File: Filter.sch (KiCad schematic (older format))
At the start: 3 parts

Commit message: Corrected connectors.
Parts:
- C9: footprint (none) -> Capacitor_SMD:C_0603_1608Metric
- R10, R11: footprint (none) -> Resistor_SMD:R_0603_1608Metric
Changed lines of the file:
@@
 F 0 "R16" H 4470 2346 50  0000 L CNN
 F 1 "10k" H 4470 2255 50  0000 L CNN
-F 2 "" V 4330 2300 50  0001 C CNN
+F 2 "Resistor_SMD:R_0603_1608Metric" V 4330 2300 50  0001 C CNN
 F 3 "~" H 4400 2300 50  0001 C CNN
 	1    4400 2300
@@
 F 0 "R15" V 3943 2550 50  0000 C CNN
 F 1 "10k" V 4034 2550 50  0000 C CNN
-F 2 "" V 4080 2550 50  0001 C CNN
+F 2 "Resistor_SMD:R_0603_1608Metric" V 4080 2550 50  0001 C CNN
 F 3 "~" H 4150 2550 50  0001 C CNN
 	1    4150 2550
@@
 F 0 "C11" H 4515 2846 50  0000 L CNN
 F 1 "10n" H 4515 2755 50  0000 L CNN
-F 2 "" H 4438 2650 50  0001 C CNN
+F 2 "Capacitor_SMD:C_0603_1608Metric" H 4438 2650 50  0001 C CNN
 F 3 "~" H 4400 2800 50  0001 C CNN
 	1    4400 2800

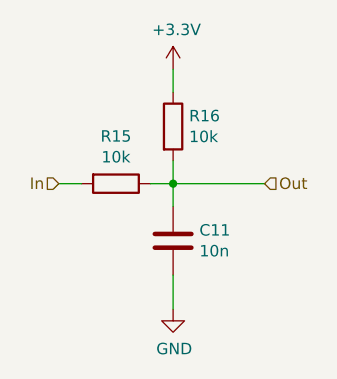
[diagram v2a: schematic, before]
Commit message: Redesigned around G431.
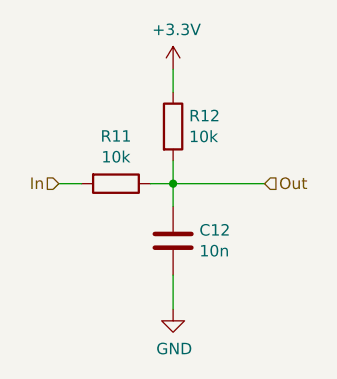
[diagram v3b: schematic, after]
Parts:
- renumbered C9 to C11, R11 to R10, R10 to R9
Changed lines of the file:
@@
 $Descr A4 11693 8268
 encoding utf-8
-Sheet 4 6
+Sheet 3 13
 Title ""
 Date ""
@@
 AR Path="/601E4198/601E449D" Ref="R?"  Part="1"
 AR Path="/601EC842/601E449D" Ref="R?"  Part="1"
-AR Path="/601ED892/601E449D" Ref="R11"  Part="1"
+AR Path="/601ED892/601E449D" Ref="R10"  Part="1"
 AR Path="/601EE918/601E449D" Ref="R?"  Part="1"
-AR Path="/601EF983/601E449D" Ref="R16"  Part="1"
+AR Path="/601EF983/601E449D" Ref="R12"  Part="1"
 AR Path="/601F09BE/601E449D" Ref="R?"  Part="1"
 AR Path="/601F1A3B/601E449D" Ref="R?"  Part="1"
@@
 AR Path="/601F6AC3/601E449D" Ref="R?"  Part="1"
 AR Path="/601F7B55/601E449D" Ref="R?"  Part="1"
-F 0 "R16" H 4470 2346 50  0000 L CNN
+AR Path="/6027857A/601E449D" Ref="R14"  Part="1"
+AR Path="/603499C2/601E449D" Ref="R16"  Part="1"
+AR Path="/603603F4/601E449D" Ref="R18"  Part="1"
+AR Path="/60382A0F/601E449D" Ref="R20"  Part="1"
+AR Path="/60398ACA/601E449D" Ref="R22"  Part="1"
+AR Path="/603AB740/601E449D" Ref="R24"  Part="1"
+AR Path="/603B0EF8/601E449D" Ref="R26"  Part="1"
+AR Path="/603B693F/601E449D" Ref="R28"  Part="1"
+AR Path="/603E1705/601E449D" Ref="R30"  Part="1"
+AR Path="/603E7B18/601E449D" Ref="R32"  Part="1"
+F 0 "R12" H 4470 2346 50  0000 L CNN
 F 1 "10k" H 4470 2255 50  0000 L CNN
 F 2 "Resistor_SMD:R_0603_1608Metric" V 4330 2300 50  0001 C CNN
@@
 AR Path="/601E4198/601E490B" Ref="R?"  Part="1"
 AR Path="/601EC842/601E490B" Ref="R?"  Part="1"
-AR Path="/601ED892/601E490B" Ref="R10"  Part="1"
+AR Path="/601ED892/601E490B" Ref="R9"  Part="1"
 AR Path="/601EE918/601E490B" Ref="R?"  Part="1"
-AR Path="/601EF983/601E490B" Ref="R15"  Part="1"
+AR Path="/601EF983/601E490B" Ref="R11"  Part="1"
 AR Path="/601F09BE/601E490B" Ref="R?"  Part="1"
 AR Path="/601F1A3B/601E490B" Ref="R?"  Part="1"
@@
 AR Path="/601F6AC3/601E490B" Ref="R?"  Part="1"
 AR Path="/601F7B55/601E490B" Ref="R?"  Part="1"
-F 0 "R15" V 3943 2550 50  0000 C CNN
+AR Path="/6027857A/601E490B" Ref="R13"  Part="1"
+AR Path="/603499C2/601E490B" Ref="R15"  Part="1"
+AR Path="/603603F4/601E490B" Ref="R17"  Part="1"
+AR Path="/60382A0F/601E490B" Ref="R19"  Part="1"
+AR Path="/60398ACA/601E490B" Ref="R21"  Part="1"
+AR Path="/603AB740/601E490B" Ref="R23"  Part="1"
+AR Path="/603B0EF8/601E490B" Ref="R25"  Part="1"
+AR Path="/603B693F/601E490B" Ref="R27"  Part="1"
+AR Path="/603E1705/601E490B" Ref="R29"  Part="1"
+AR Path="/603E7B18/601E490B" Ref="R31"  Part="1"
+F 0 "R11" V 3943 2550 50  0000 C CNN
 F 1 "10k" V 4034 2550 50  0000 C CNN
 F 2 "Resistor_SMD:R_0603_1608Metric" V 4080 2550 50  0001 C CNN
@@
 AR Path="/601ED892/601E5AA9" Ref="#PWR030"  Part="1"
 AR Path="/601EE918/601E5AA9" Ref="#PWR?"  Part="1"
-AR Path="/601EF983/601E5AA9" Ref="#PWR034"  Part="1"
+AR Path="/601EF983/601E5AA9" Ref="#PWR032"  Part="1"
 AR Path="/601F09BE/601E5AA9" Ref="#PWR?"  Part="1"
 AR Path="/601F1A3B/601E5AA9" Ref="#PWR?"  Part="1"
@@
 AR Path="/601F6AC3/601E5AA9" Ref="#PWR?"  Part="1"
 AR Path="/601F7B55/601E5AA9" Ref="#PWR?"  Part="1"
-F 0 "#PWR034" H 4400 1900 50  0001 C CNN
+AR Path="/6027857A/601E5AA9" Ref="#PWR034"  Part="1"
+AR Path="/603499C2/601E5AA9" Ref="#PWR036"  Part="1"
+AR Path="/603603F4/601E5AA9" Ref="#PWR038"  Part="1"
+AR Path="/60382A0F/601E5AA9" Ref="#PWR040"  Part="1"
+AR Path="/60398ACA/601E5AA9" Ref="#PWR042"  Part="1"
+AR Path="/603AB740/601E5AA9" Ref="#PWR044"  Part="1"
+AR Path="/603B0EF8/601E5AA9" Ref="#PWR046"  Part="1"
+AR Path="/603B693F/601E5AA9" Ref="#PWR048"  Part="1"
+AR Path="/603E1705/601E5AA9" Ref="#PWR050"  Part="1"
+AR Path="/603E7B18/601E5AA9" Ref="#PWR052"  Part="1"
+F 0 "#PWR032" H 4400 1900 50  0001 C CNN
 F 1 "+3.3V" H 4415 2223 50  0000 C CNN
 F 2 "" H 4400 2050 50  0001 C CNN
@@
 AR Path="/601E4198/601E64F4" Ref="C?"  Part="1"
 AR Path="/601EC842/601E64F4" Ref="C?"  Part="1"
-AR Path="/601ED892/601E64F4" Ref="C9"  Part="1"
+AR Path="/601ED892/601E64F4" Ref="C11"  Part="1"
 AR Path="/601EE918/601E64F4" Ref="C?"  Part="1"
-AR Path="/601EF983/601E64F4" Ref="C11"  Part="1"
+AR Path="/601EF983/601E64F4" Ref="C12"  Part="1"
 AR Path="/601F09BE/601E64F4" Ref="C?"  Part="1"
 AR Path="/601F1A3B/601E64F4" Ref="C?"  Part="1"
@@
 AR Path="/601F6AC3/601E64F4" Ref="C?"  Part="1"
 AR Path="/601F7B55/601E64F4" Ref="C?"  Part="1"
-F 0 "C11" H 4515 2846 50  0000 L CNN
+AR Path="/6027857A/601E64F4" Ref="C13"  Part="1"
+AR Path="/603499C2/601E64F4" Ref="C14"  Part="1"
+AR Path="/603603F4/601E64F4" Ref="C15"  Part="1"
+AR Path="/60382A0F/601E64F4" Ref="C16"  Part="1"
+AR Path="/60398ACA/601E64F4" Ref="C17"  Part="1"
+AR Path="/603AB740/601E64F4" Ref="C18"  Part="1"
+AR Path="/603B0EF8/601E64F4" Ref="C19"  Part="1"
+AR Path="/603B693F/601E64F4" Ref="C20"  Part="1"
+AR Path="/603E1705/601E64F4" Ref="C21"  Part="1"
+AR Path="/603E7B18/601E64F4" Ref="C22"  Part="1"
+F 0 "C12" H 4515 2846 50  0000 L CNN
 F 1 "10n" H 4515 2755 50  0000 L CNN
 F 2 "Capacitor_SMD:C_0603_1608Metric" H 4438 2650 50  0001 C CNN
@@
 AR Path="/601ED892/601E7218" Ref="#PWR031"  Part="1"
 AR Path="/601EE918/601E7218" Ref="#PWR?"  Part="1"
-AR Path="/601EF983/601E7218" Ref="#PWR035"  Part="1"
+AR Path="/601EF983/601E7218" Ref="#PWR033"  Part="1"
 AR Path="/601F09BE/601E7218" Ref="#PWR?"  Part="1"
 AR Path="/601F1A3B/601E7218" Ref="#PWR?"  Part="1"
@@
 AR Path="/601F6AC3/601E7218" Ref="#PWR?"  Part="1"
 AR Path="/601F7B55/601E7218" Ref="#PWR?"  Part="1"
-F 0 "#PWR035" H 4400 2850 50  0001 C CNN
+AR Path="/6027857A/601E7218" Ref="#PWR035"  Part="1"
+AR Path="/603499C2/601E7218" Ref="#PWR037"  Part="1"
+AR Path="/603603F4/601E7218" Ref="#PWR039"  Part="1"
+AR Path="/60382A0F/601E7218" Ref="#PWR041"  Part="1"
+AR Path="/60398ACA/601E7218" Ref="#PWR043"  Part="1"
+AR Path="/603AB740/601E7218" Ref="#PWR045"  Part="1"
+AR Path="/603B0EF8/601E7218" Ref="#PWR047"  Part="1"
+AR Path="/603B693F/601E7218" Ref="#PWR049"  Part="1"
+AR Path="/603E1705/601E7218" Ref="#PWR051"  Part="1"
+AR Path="/603E7B18/601E7218" Ref="#PWR053"  Part="1"
+F 0 "#PWR033" H 4400 2850 50  0001 C CNN
 F 1 "GND" H 4405 2927 50  0000 C CNN
 F 2 "" H 4400 3100 50  0001 C CNN

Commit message: Minor adjustments.
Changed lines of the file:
@@
 $Descr A4 11693 8268
 encoding utf-8
-Sheet 3 13
+Sheet 5 13
 Title ""
 Date ""
@@
 AR Path="/603E1705/601E449D" Ref="R30"  Part="1"
 AR Path="/603E7B18/601E449D" Ref="R32"  Part="1"
-F 0 "R12" H 4470 2346 50  0000 L CNN
+F 0 "R16" H 4470 2346 50  0000 L CNN
 F 1 "10k" H 4470 2255 50  0000 L CNN
 F 2 "Resistor_SMD:R_0603_1608Metric" V 4330 2300 50  0001 C CNN
@@
 AR Path="/603E1705/601E490B" Ref="R29"  Part="1"
 AR Path="/603E7B18/601E490B" Ref="R31"  Part="1"
-F 0 "R11" V 3943 2550 50  0000 C CNN
+F 0 "R15" V 3943 2550 50  0000 C CNN
 F 1 "10k" V 4034 2550 50  0000 C CNN
 F 2 "Resistor_SMD:R_0603_1608Metric" V 4080 2550 50  0001 C CNN
@@
 AR Path="/603E1705/601E5AA9" Ref="#PWR050"  Part="1"
 AR Path="/603E7B18/601E5AA9" Ref="#PWR052"  Part="1"
-F 0 "#PWR032" H 4400 1900 50  0001 C CNN
+F 0 "#PWR052" H 4400 1900 50  0001 C CNN
 F 1 "+3.3V" H 4415 2223 50  0000 C CNN
 F 2 "" H 4400 2050 50  0001 C CNN
@@
 AR Path="/603E1705/601E64F4" Ref="C21"  Part="1"
 AR Path="/603E7B18/601E64F4" Ref="C22"  Part="1"
-F 0 "C12" H 4515 2846 50  0000 L CNN
+F 0 "C14" H 4515 2846 50  0000 L CNN
 F 1 "10n" H 4515 2755 50  0000 L CNN
 F 2 "Capacitor_SMD:C_0603_1608Metric" H 4438 2650 50  0001 C CNN
@@
 AR Path="/603E1705/601E7218" Ref="#PWR051"  Part="1"
 AR Path="/603E7B18/601E7218" Ref="#PWR053"  Part="1"
-F 0 "#PWR033" H 4400 2850 50  0001 C CNN
+F 0 "#PWR053" H 4400 2850 50  0001 C CNN
 F 1 "GND" H 4405 2927 50  0000 C CNN
 F 2 "" H 4400 3100 50  0001 C CNN

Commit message: Final layout.
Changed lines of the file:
@@
 $Descr A4 11693 8268
 encoding utf-8
-Sheet 5 13
+Sheet 7 13
 Title ""
 Date ""
@@
 AR Path="/603E1705/601E449D" Ref="R30"  Part="1"
 AR Path="/603E7B18/601E449D" Ref="R32"  Part="1"
-F 0 "R16" H 4470 2346 50  0000 L CNN
+F 0 "R20" H 4470 2346 50  0000 L CNN
 F 1 "10k" H 4470 2255 50  0000 L CNN
 F 2 "Resistor_SMD:R_0603_1608Metric" V 4330 2300 50  0001 C CNN
@@
 AR Path="/603E1705/601E490B" Ref="R29"  Part="1"
 AR Path="/603E7B18/601E490B" Ref="R31"  Part="1"
-F 0 "R15" V 3943 2550 50  0000 C CNN
+F 0 "R19" V 3943 2550 50  0000 C CNN
 F 1 "10k" V 4034 2550 50  0000 C CNN
 F 2 "Resistor_SMD:R_0603_1608Metric" V 4080 2550 50  0001 C CNN
@@
 AR Path="/603E1705/601E5AA9" Ref="#PWR050"  Part="1"
 AR Path="/603E7B18/601E5AA9" Ref="#PWR052"  Part="1"
-F 0 "#PWR052" H 4400 1900 50  0001 C CNN
+F 0 "#PWR040" H 4400 1900 50  0001 C CNN
 F 1 "+3.3V" H 4415 2223 50  0000 C CNN
 F 2 "" H 4400 2050 50  0001 C CNN
@@
 AR Path="/603E1705/601E64F4" Ref="C21"  Part="1"
 AR Path="/603E7B18/601E64F4" Ref="C22"  Part="1"
-F 0 "C14" H 4515 2846 50  0000 L CNN
+F 0 "C16" H 4515 2846 50  0000 L CNN
 F 1 "10n" H 4515 2755 50  0000 L CNN
 F 2 "Capacitor_SMD:C_0603_1608Metric" H 4438 2650 50  0001 C CNN
@@
 AR Path="/603E1705/601E7218" Ref="#PWR051"  Part="1"
 AR Path="/603E7B18/601E7218" Ref="#PWR053"  Part="1"
-F 0 "#PWR053" H 4400 2850 50  0001 C CNN
+F 0 "#PWR041" H 4400 2850 50  0001 C CNN
 F 1 "GND" H 4405 2927 50  0000 C CNN
 F 2 "" H 4400 3100 50  0001 C CNN
